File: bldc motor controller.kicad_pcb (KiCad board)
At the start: 6 copper layers, 47 parts

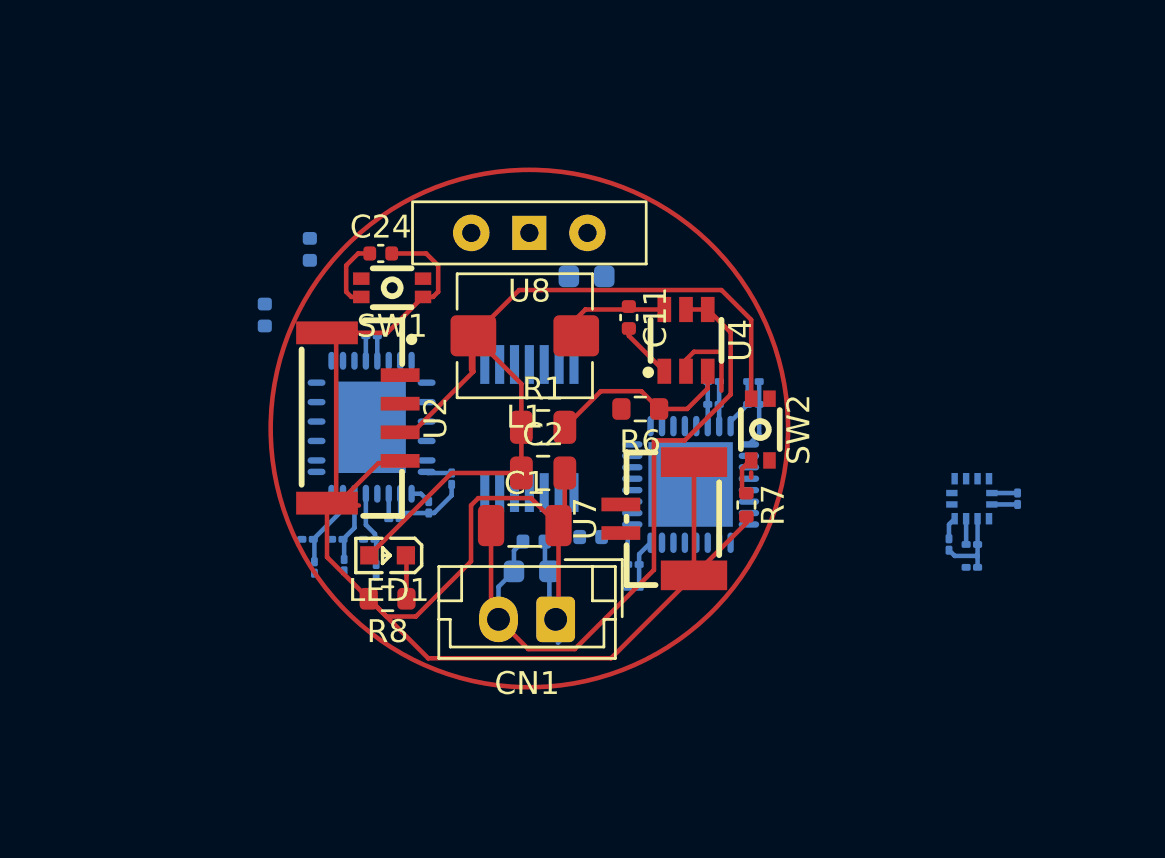
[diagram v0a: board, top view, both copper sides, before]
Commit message: I give up it'll be a 4 layer
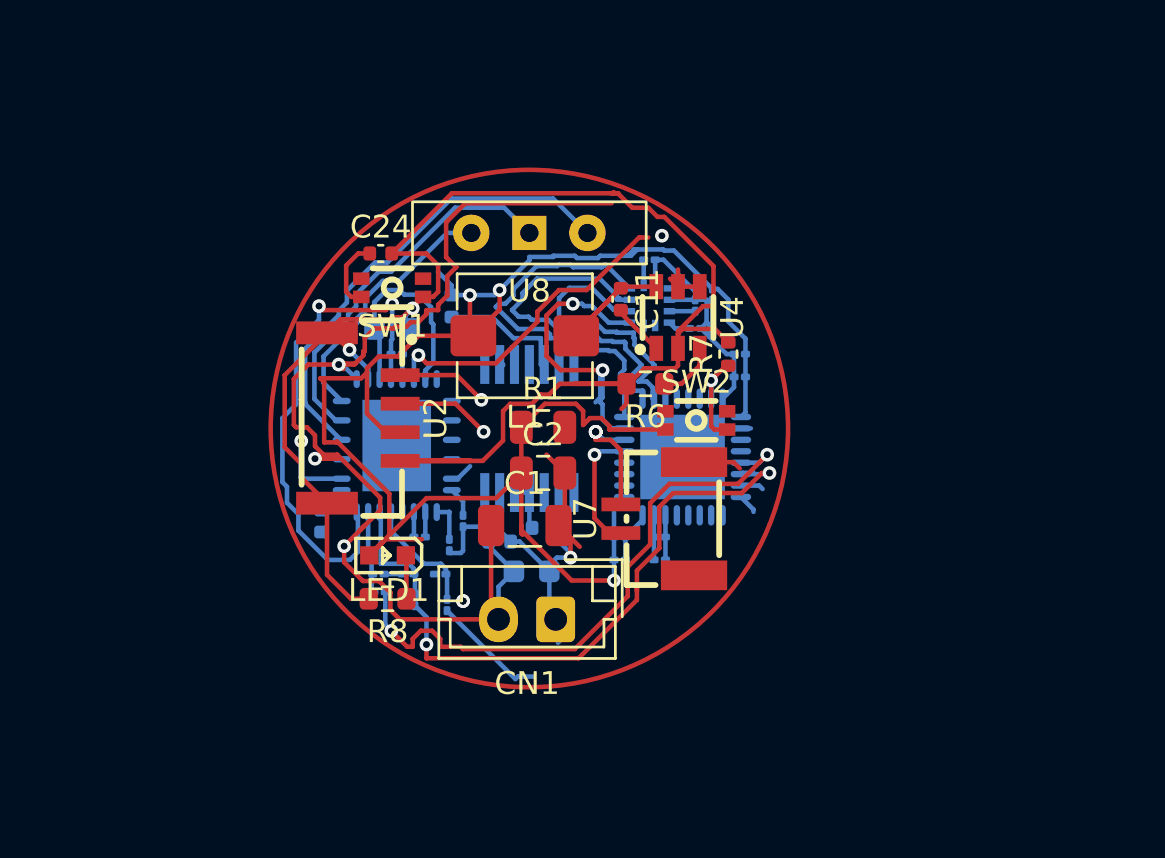
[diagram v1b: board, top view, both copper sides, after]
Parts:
- moved C20 19.2 mm to (153.2, 80.0), turned to 0 degrees
- moved C22 16.5 mm to (156.0, 81.5), turned to -90 degrees
- moved U6 16.4 mm to (153.2, 82.0), turned to 90 degrees
- moved C23 16.0 mm to (155.2, 82.0), turned to 90 degrees
- moved C21 14.6 mm to (155.2, 83.0), turned to 0 degrees
- moved C10 11.9 mm to (138.9, 91.4), turned to 90 degrees
- moved C17 11.2 mm to (157.2, 84.1), turned to 0 degrees
- moved C15 9.75 mm to (151.9, 93.1), turned to 180 degrees
- moved C16 9.43 mm to (157.2, 85.1), turned to 0 degrees
- moved C7 8.81 mm to (142.0, 83.0)
- moved C14 8.24 mm to (151.9, 92.1), turned to 180 degrees
- moved C18 8.18 mm to (144.6, 82.0), turned to 90 degrees
- moved C12 8.15 mm to (153.7, 93.1), turned to 180 degrees
- moved R7 6.65 mm to (156.7, 84.1), turned to 90 degrees
- moved C13 6.26 mm to (153.7, 92.1), turned to 180 degrees
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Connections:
- U8 pad 1: PHASE-A -> PHASE-B
- U8 pad 2: PHASE-B -> PHASE-A
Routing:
- net TI_VREF: track 48.6 -> 87.1 mm, vias 0 -> 3
- net TI_AGND: track 95.4 -> 132.7 mm, vias 0 -> 4
- net SOA: track 0.00 -> 26.2 mm, vias 0 -> 2
- net SOB: track 0.00 -> 24.9 mm, vias 0 -> 2
- net +BATT: track 31.8 -> 54.9 mm, vias 0 -> 3
- net I-LIMIT: track 1.09 -> 22.5 mm, vias 0 -> 2
- net PHASE-A: track 0.00 -> 20.8 mm
- net SDA1: track 0.00 -> 16.6 mm
- net PHASE-B: track 0.00 -> 16.5 mm
- net ENAB_MAG: track 0.00 -> 15.5 mm
- net TI_FAULT: track 0.00 -> 14.1 mm, vias 0 -> 1
- net SCL1: track 0.00 -> 13.5 mm, vias 0 -> 2
- net ENAB_XL: track 0.00 -> 12.0 mm
- net PHASE-C: track 0.00 -> 11.4 mm
- net TI_AVDD: track 0.00 -> 9.98 mm
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
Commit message: Almost done design, need to add mounting holes I think
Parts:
- added REF**: MountingHole_2.2mm_M2_ISO14580_Pad, MountingHole:MountingHole_2.2mm_M2_ISO14580_Pad, F.Cu at (152.4, 74.5)
- C1, C11, C2, L1, R1, R6, U4: moved to B.Cu
- C10, C18, C3, C4, C5, C6, C7, R10, R11, R2, R3, R4, R9, U1: moved to F.Cu
- C19: footprint Capacitor_SMD:C_0402_1005Metric -> Capacitor_SMD:C_01005_0402Metric
- U2: footprint bldc-motor-footprints:CONN-SMD_4P-P1.25_SM04B-GHS-TB-LF-SN -> Connector_JST:JST_ACH_BM04B-ACHSS-A-GAN-ETF_1x04-1MP_P1.20mm_Vertical
- U7: footprint bldc-motor-footprints:CONN-SMD_SM02B-GHS-TB-LF-SN -> Connector_JST:JST_GH_BM02B-GHS-TBT_1x02-1MP_P1.25mm_Vertical
- U8: footprint Button_Switch_THT:SW_Slide-03_Wuerth-WS-SLTV_10x2.5x6.4_P2.54mm -> Connector_PinHeader_2.54mm:PinHeader_1x03_P2.54mm_Vertical
- moved U4 20.3 mm to (136.4, 91.8), turned to 180 degrees
- moved C11 20.3 mm to (136.8, 95.1), turned to 180 degrees
- moved C18 15.4 mm to (134.7, 93.8), turned to 0 degrees
- moved C2 14.4 mm to (136.3, 81.8)
- moved R7 13.9 mm to (143.9, 89.5), turned to 180 degrees
- moved L1 12.6 mm to (135.6, 86.4), turned to 90 degrees
- moved C24 12.2 mm to (142.2, 91.9), turned to 90 degrees
- moved R10 12.2 mm to (132.9, 90.8)
- moved R6 11.8 mm to (141.7, 82.3), turned to 90 degrees
- moved SW2 11.1 mm to (144.9, 91.0), turned to 180 degrees
- moved R9 10.9 mm to (133.6, 92.0)
- moved SW1 10.8 mm to (140.8, 91.9), turned to -90 degrees
- moved R1 10.2 mm to (139.8, 82.2), turned to -90 degrees
- moved C22 9.25 mm to (146.9, 80.0), turned to 180 degrees
- moved C21 9.19 mm to (146.8, 79.3), turned to 180 degrees
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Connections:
- C10 pad 2: Net-(U1-CP) -> TI_AVDD
- U1 pad 1: Net-(U1-CP) -> TI_AVDD
- U8 pad 1: PHASE-B -> PHASE-A
- U8 pad 2: PHASE-A -> PHASE-B
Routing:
- net TI_AGND: track 132.7 -> 184.4 mm, vias 4 -> 10
- net +BATT: track 54.9 -> 25.2 mm, vias 3 -> 2
- net NSS1: track 0.00 -> 29.7 mm, vias 0 -> 2
- net TIM1_CH3N: track 1.46 -> 26.6 mm, vias 0 -> 2
- net TIM1_CH1N: track 0.00 -> 22.7 mm, vias 0 -> 2
- net TIM1_CH2N: track 0.00 -> 20.6 mm, vias 0 -> 2
- net TIM1_CH2: track 0.00 -> 19.9 mm, vias 0 -> 2
- net TIM1_CH1: track 0.00 -> 17.0 mm, vias 0 -> 2
- net TIM1_CH3: track 0.00 -> 16.7 mm, vias 0 -> 2
- net MISO1: track 0.00 -> 16.4 mm, vias 0 -> 2
- net TI_VREF: track 87.1 -> 101.7 mm, vias 3 -> 4
- net SCK1: track 0.19 -> 14.8 mm, vias 0 -> 2
- net UART_RX: track 5.04 -> 19.5 mm, vias 1 -> 2
- net MOSI1: track 0.00 -> 14.1 mm, vias 0 -> 2
- net TI_FAULT: track 14.1 -> 27.9 mm, vias 1 -> 2
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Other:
- copper layers 6 -> 4

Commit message: yeee haw
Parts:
- added REF**: MountingHole_2.2mm_M2_ISO14580_Pad, MountingHole:MountingHole_2.2mm_M2_ISO14580_Pad, F.Cu at (149.2, 79.8)
- moved REF** 27.2 mm to (136.5, 96.6)
- moved LED1 4.11 mm to (144.6, 94.0), turned to 180 degrees
- moved C21 3.17 mm to (146.2, 82.4), turned to -90 degrees
- moved R8 2.80 mm to (147.6, 92.7)
- moved C22 2.35 mm to (146.9, 82.3), turned to -90 degrees
- moved U3 2.20 mm to (149.8, 89.9)
- moved C12 2.20 mm to (148.0, 94.6)
- moved C13 2.20 mm to (148.0, 93.8)
- moved C14 2.20 mm to (146.3, 92.6)
- moved C15 2.20 mm to (147.0, 92.6)
- moved C20 2.20 mm to (146.3, 84.3)
- moved U6 2.20 mm to (148.0, 84.3)
- moved C16 2.07 mm to (151.8, 86.2)
- moved C17 1.94 mm to (151.8, 85.4)
- moved C18 1.81 mm to (132.9, 93.6)
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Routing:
- net TI_AGND: track 184.4 -> 159.4 mm, vias 10 -> 8
- net +BATT: track 25.2 -> 47.6 mm
- net TI_AVDD: track 17.2 -> 30.9 mm, vias 2 -> 3
- net SOA: track 17.7 -> 26.3 mm, vias 2 -> 1
- net TIM1_CH1: track 17.0 -> 24.6 mm
- net SOC: track 16.5 -> 23.4 mm
- net SCL1: track 6.06 -> 12.7 mm
- net TI_FAULT: track 27.9 -> 34.4 mm
- net BOOT0: track 14.6 -> 21.0 mm
- net TIM1_CH3N: track 26.6 -> 32.3 mm
- net NSS1: track 29.7 -> 34.2 mm
- net CAN_TX: track 6.28 -> 10.2 mm
- net (no net): track 3.50 -> 0.00 mm
- net TI_VREF: track 101.7 -> 98.5 mm, vias 4 -> 3
- net TIM1_CH2N: track 20.6 -> 23.7 mm
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- added copper zone on B.Cu, net TI_AGND
- added copper zone on F.Cu, net TI_AGND
- added copper zone on In1.Cu, net TI_AGND
- added copper zone on In2.Cu, net TI_AGND
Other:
- board outline added: 26 x 26 mm

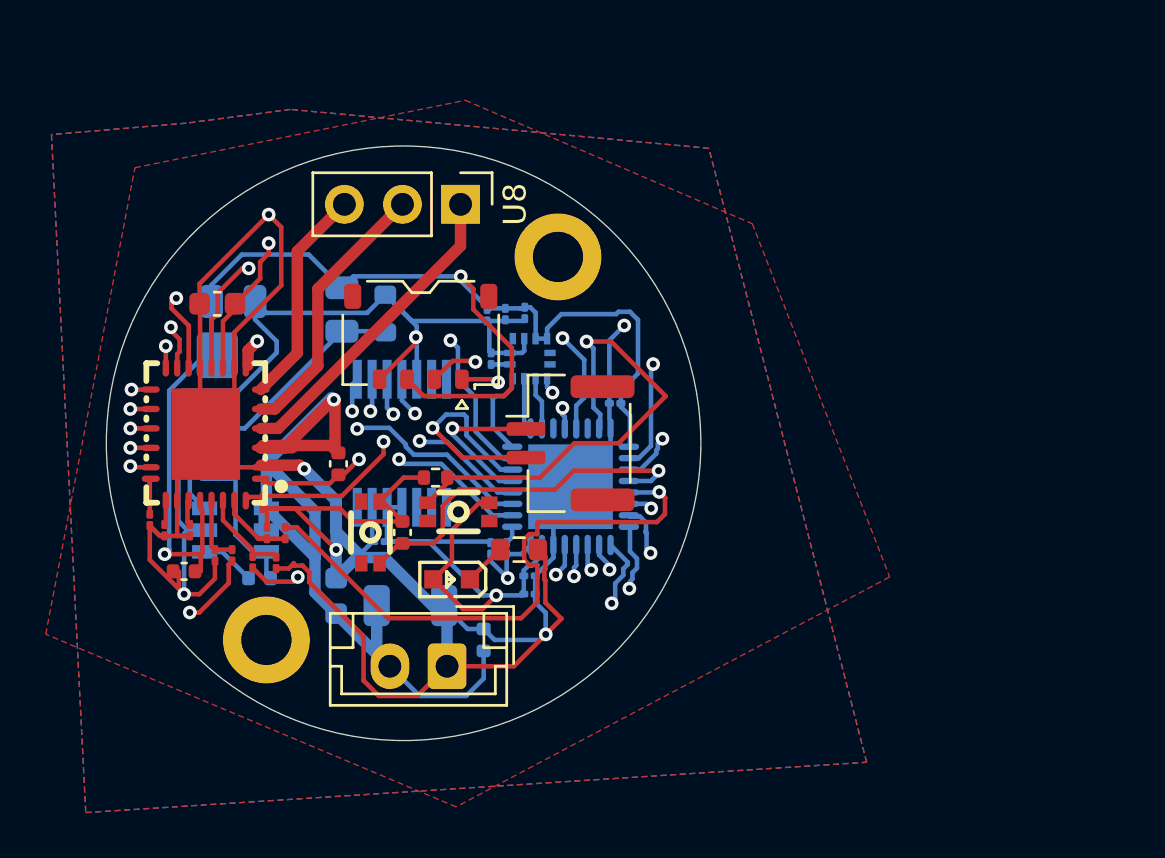
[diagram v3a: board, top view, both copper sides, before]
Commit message: Power Ground Signal Ground Seperate
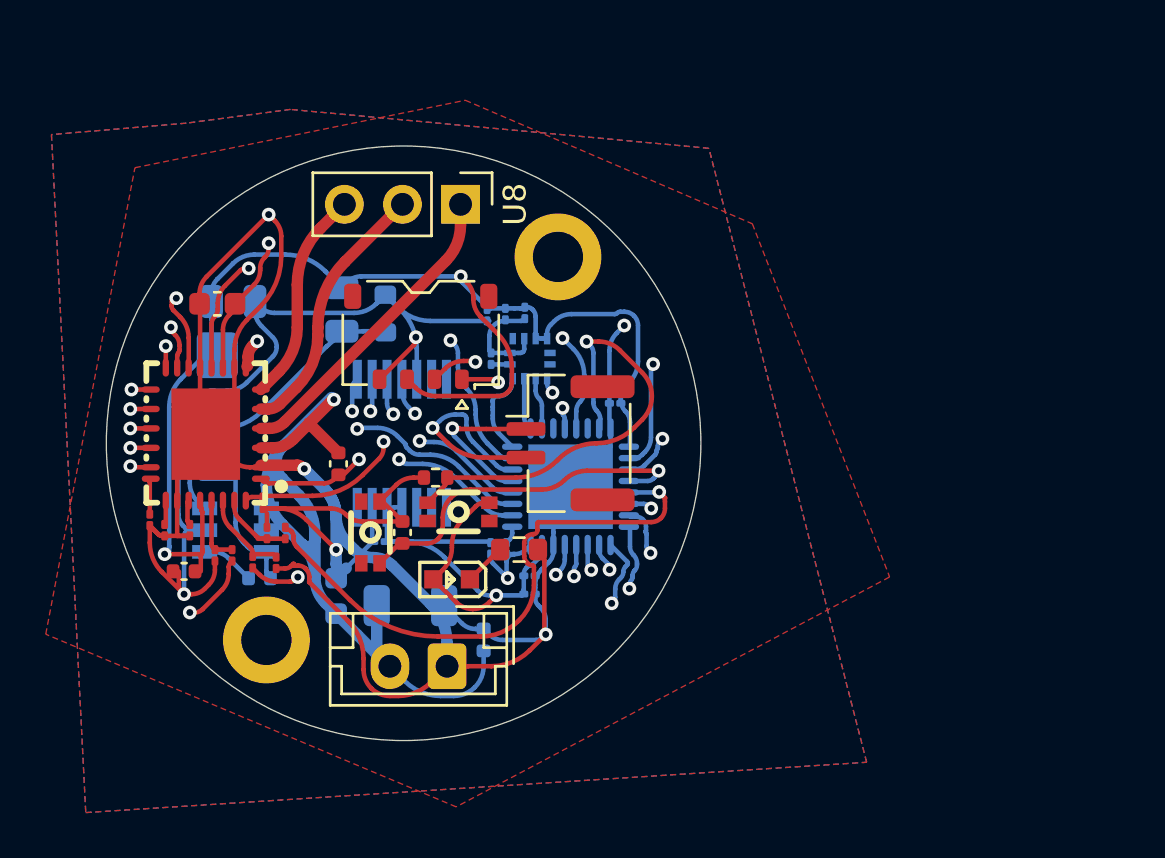
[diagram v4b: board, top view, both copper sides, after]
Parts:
- C21, C23: value C_Small -> 100nF
- C22: value C_Small -> 10uF
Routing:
- net TI_AGND: track 159.4 -> 153.6 mm
- net +BATT: track 47.6 -> 44.2 mm
- net TI_VREF: track 98.5 -> 96.4 mm
- net TIM1_CH3N: track 32.3 -> 30.9 mm
- net BOOT0: track 21.0 -> 19.8 mm
- net TIM1_CH1: track 24.6 -> 23.5 mm
- net NSS1: track 34.2 -> 33.3 mm
- net I-LIMIT: track 26.3 -> 25.5 mm
- net TI_AVDD: track 30.9 -> 30.2 mm
- net TIM1_CH1N: track 25.5 -> 24.9 mm
- net TIM1_CH2N: track 23.7 -> 23.1 mm
- net TI_FAULT: track 34.4 -> 33.8 mm
- net SOA: track 26.3 -> 25.8 mm

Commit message: 4 layer nice looking board
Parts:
- removed CN1: ~, Connector_JST:JST_EH_B2B-EH-A_1x02_P2.50mm_Vertical
- removed REF** (x2): MountingHole_2.2mm_M2_ISO14580_Pad, MountingHole:MountingHole_2.2mm_M2_ISO14580_Pad
- removed U2: ~, Connector_JST:JST_ACH_BM04B-ACHSS-A-GAN-ETF_1x04-1MP_P1.20mm_Vertical
- added -BAT+1: ~, Connector_JST:JST_EH_B2B-EH-A_1x02_P2.50mm_Vertical, F.Cu at (140.9, 96.8)
- added J1: Conn_01x04_Pin, Connector_PinHeader_1.00mm:PinHeader_1x04_P1.00mm_Vertical, F.Cu at (145.6, 85.0)
- added M2: MountingHole_2.2mm_M2_DIN965_Pad, MountingHole:MountingHole_2.2mm_M2_DIN965_Pad, F.Cu at (136.0, 79.9)
- added M2: MountingHole_2.2mm_M2_DIN965_Pad, MountingHole:MountingHole_2.2mm_M2_DIN965_Pad, F.Cu at (148.8, 96.3)
- added NT1: NetTie_2, NetTie:NetTie-2_SMD_Pad0.5mm, B.Cu at (135.8, 93.0)
- C22: footprint Capacitor_SMD:C_01005_0402Metric -> Capacitor_SMD:C_0603_1608Metric
- C8: moved to F.Cu
- LED1: footprint bldc-motor-footprints:LED0603-RD -> LED_SMD:LED_0603_1608Metric
- U1: value ~ -> C47023655
- U3: value ~ -> C529358
- U6: value ~ -> C126671
- moved R6 14.6 mm to (137.9, 96.5), turned to 0 degrees
- moved C8 14.4 mm to (142.3, 82.7), turned to -90 degrees
- moved R8 11.6 mm to (136.3, 95.4)
- moved C18 10.5 mm to (142.8, 90.0), turned to 90 degrees
- moved C12 10.3 mm to (151.1, 84.8), turned to 0 degrees
- moved C13 10.2 mm to (151.1, 84.1), turned to 0 degrees
- moved R4 10.1 mm to (144.0, 88.2), turned to 0 degrees
- moved C15 9.86 mm to (152.8, 84.7), turned to 0 degrees
- moved C14 9.84 mm to (152.8, 85.2), turned to 0 degrees
- moved C5 9.73 mm to (142.8, 88.2), turned to 0 degrees
- moved R3 9.63 mm to (143.1, 86.8), turned to 0 degrees
- moved R9 9.63 mm to (141.6, 90.2), turned to 0 degrees
- moved R10 9.21 mm to (140.6, 91.8), turned to 0 degrees
- moved LED1 8.83 mm to (136.3, 97.1), turned to 0 degrees
- moved R11 8.78 mm to (141.6, 89.2), turned to 0 degrees
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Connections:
- C1 pad 2: TI_AGND -> -BATT
- C8 pad 2: TI_AGND -> -BATT
- C9 pad 2: TI_AGND -> -BATT
- R6 pad 2: TI_AGND -> -BATT
- U1 pad 2: TI_AGND -> -BATT
- U4 pad 2: TI_AGND -> -BATT
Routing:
- net TI_AGND: track 153.6 -> 84.7 mm, vias 8 -> 9
- net -BATT: track 0.00 -> 48.4 mm, vias 0 -> 1
- net TI_VREF: track 96.4 -> 136.1 mm, vias 3 -> 5
- net +BATT: track 44.2 -> 77.4 mm, vias 2 -> 3
- net SOA: track 25.8 -> 6.56 mm
- net NSS1: track 33.3 -> 15.8 mm
- net SOB: track 20.8 -> 4.44 mm, vias 2 -> 1
- net BOOT0: track 19.8 -> 3.51 mm
- net TIM1_CH3N: track 30.9 -> 14.9 mm
- net ENAB_MAG: track 2.27 -> 17.2 mm, vias 0 -> 2
- net TI_FAULT: track 33.8 -> 19.4 mm
- net UART_RX: track 17.4 -> 3.06 mm, vias 2 -> 0
- net SDA1: track 3.75 -> 17.7 mm, vias 0 -> 2
- net ENAB_XL: track 2.24 -> 14.6 mm, vias 0 -> 2
- net TIM1_CH2N: track 23.1 -> 35.4 mm
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- removed copper zone on B.Cu, net TI_AGND
- removed copper zone on F.Cu, net TI_AGND
- removed copper zone on In2.Cu, net TI_AGND
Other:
- board text added: "A B C"
- board text added: "BOOT"
- board text added: "CAN"
- board text added: "RST"
- board text added: "RX TX"

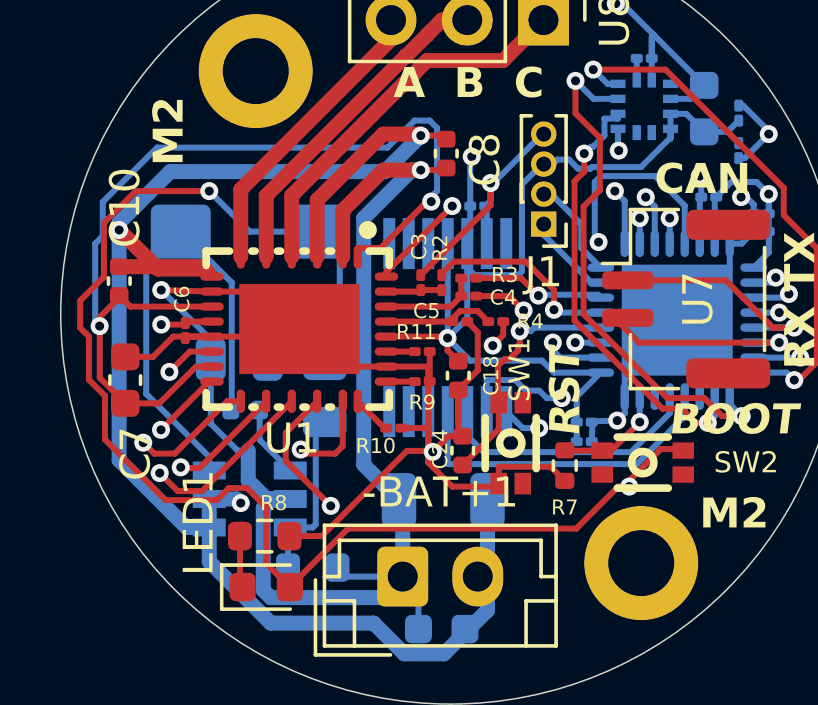
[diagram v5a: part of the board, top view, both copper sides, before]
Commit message: resistor for current sense did not exist
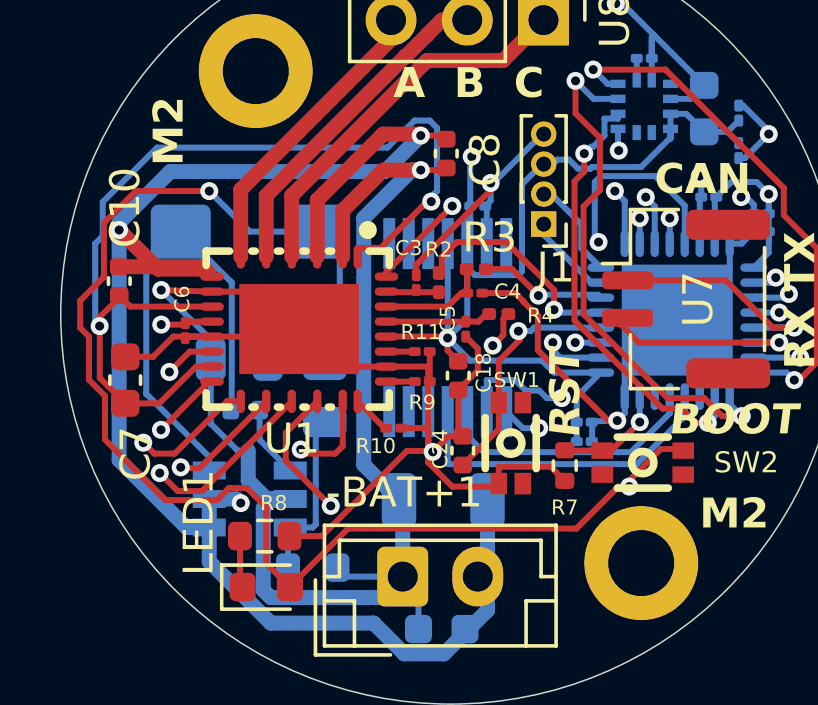
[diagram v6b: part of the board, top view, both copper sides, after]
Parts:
- R2, R3, R4: footprint Resistor_SMD:R_01005_0402Metric -> Resistor_SMD:R_0201_0603Metric
- moved R3 0.39 mm to (143.3, 86.5)
- moved C5 0.32 mm to (143.0, 88.5), turned to -90 degrees
- moved R4 0.27 mm to (144.1, 88.0)
- moved C4 0.22 mm to (143.3, 87.3)
- moved C3 0.15 mm to (141.3, 87.0)
- moved R2 0.10 mm to (142.1, 87.0)
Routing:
- net TI_AGND: track 84.7 -> 77.4 mm, vias 9 -> 8
- net SOA: track 6.56 -> 7.42 mm
